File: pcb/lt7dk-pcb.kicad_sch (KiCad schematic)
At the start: 43 parts, among them J1 PINHD_1x8_Male, J2 Conn_01x02, J3 PINHD_1x2_Male, J4 PINHD_1x2_Male, J5 PINHD_1x2_Male, J6 PINHD_1x2_Male, SW1 SW_Push, SW2 SW_Push, SW3 SW_Push, SW4 SW_Push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

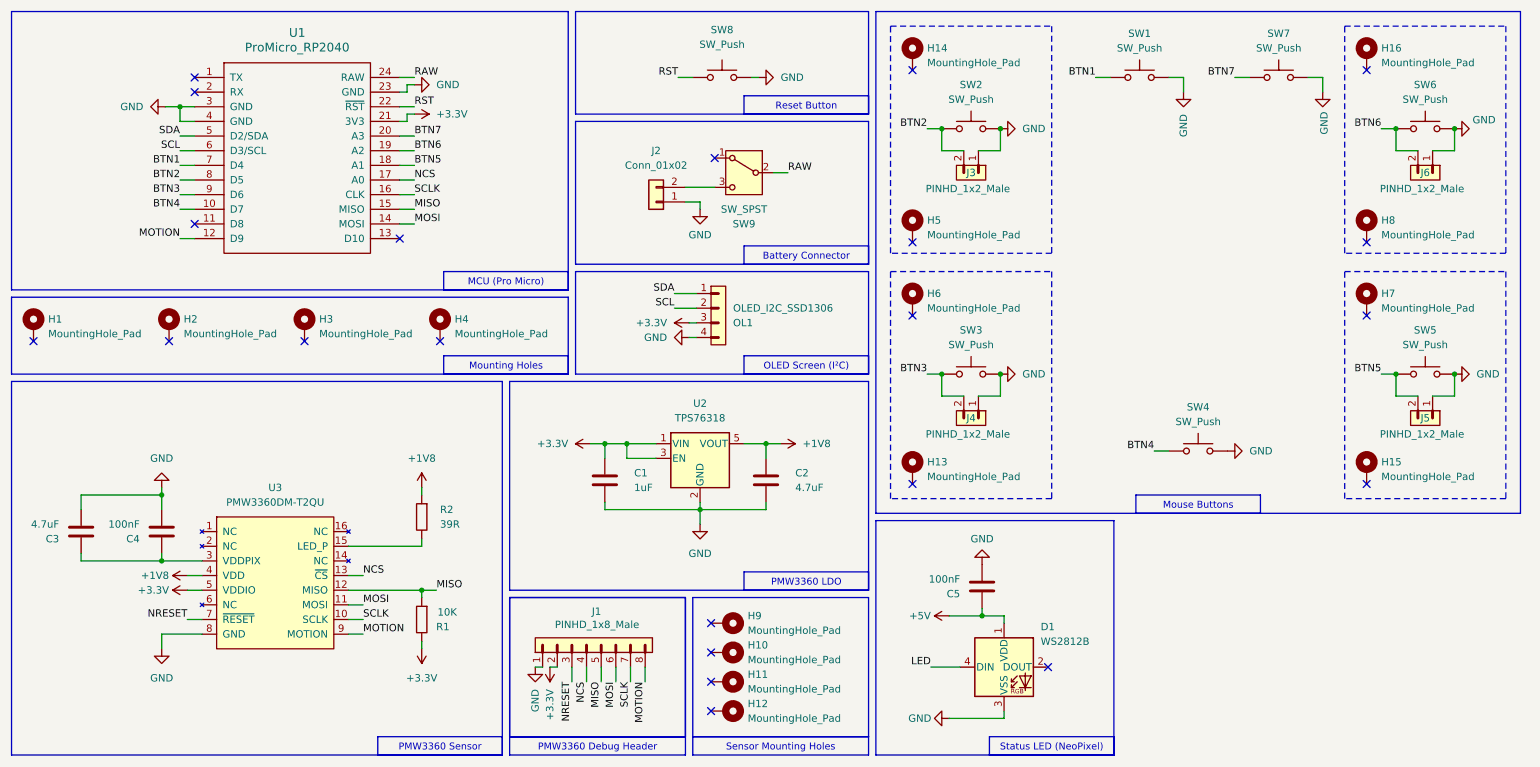
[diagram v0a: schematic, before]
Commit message: Update mouse bites & add some silkscreen info
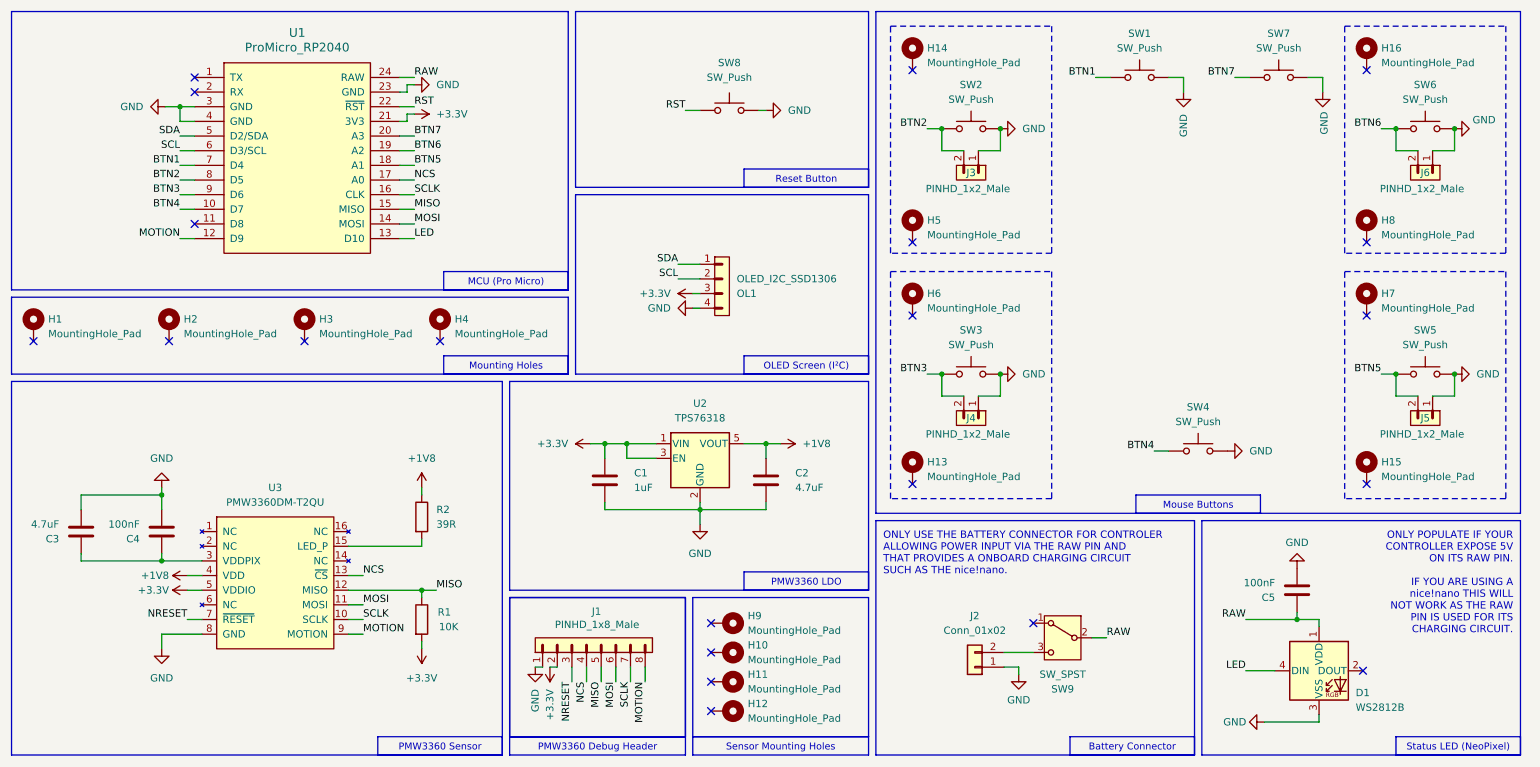
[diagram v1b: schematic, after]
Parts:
- R1, R2: symbol PCM_SL_Resistors:Resistor -> Device:R
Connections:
- net +5V is gone; now on net RAW: C5.2, D1.1 (VDD)
- net LED: now also U1.13 (D10)
- no-connect marks 22 -> 21
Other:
- note added: "ONLY POPULATE IF YOUR CONTROLLER EXPOSE 5V ON ITS RAW PIN. IF YOU ARE USING A nice!nano THIS WILL NOT WORK AS THE RAW PIN IS USED FOR ITS CHARGING CIRCUIT."
- note added: "ONLY USE THE BATTERY CONNECTOR FOR CONTROLER ALLOWING POWER INPUT VIA THE RAW PIN AND THAT PROVIDES A ONBOARD CHARGING CIRCUIT SUCH AS THE nice!nano."
- moved on the sheet: C5, D1, OL1, R1, R2, SW8

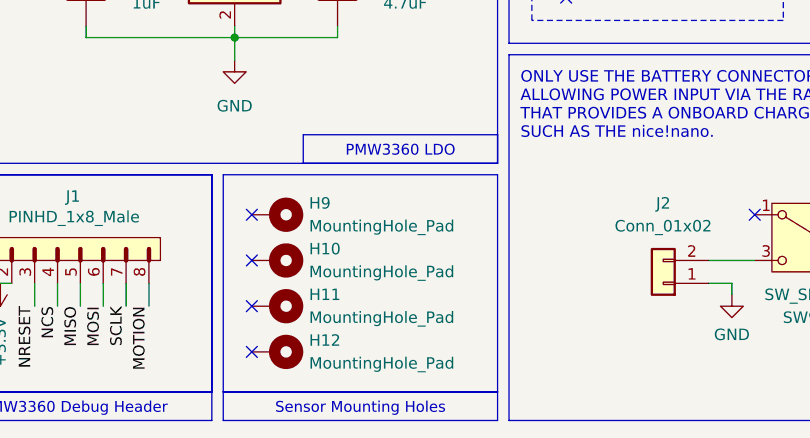
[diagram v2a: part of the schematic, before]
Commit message: Upgrade project to KiCad 9 (#3)
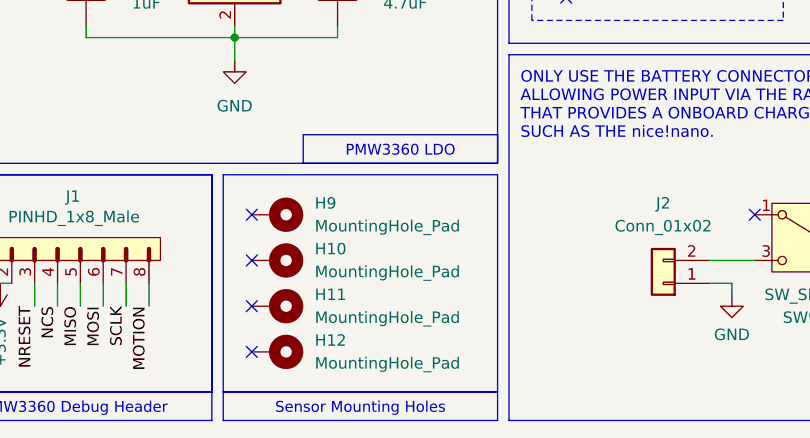
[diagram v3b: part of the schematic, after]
